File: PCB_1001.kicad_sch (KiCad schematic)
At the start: 3 parts

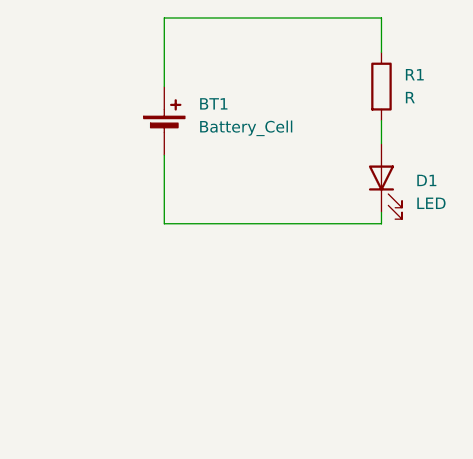
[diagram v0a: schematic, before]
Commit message: VTPN applied, incl footprints
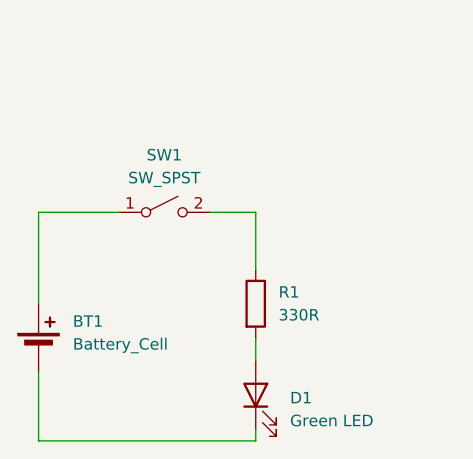
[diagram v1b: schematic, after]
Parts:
- added SW1: SW_SPST, symbol Switch:SW_SPST
- D1: value LED -> Green LED; footprint (none) -> LED_SMD:LED_0805_2012Metric; MFG (none) -> Dialight; MPN (none) -> 598-8181-102F; VTPN (none) -> 4752-01010-00
- R1: value R -> 330R; footprint (none) -> Resistor_SMD:R_0603_1608Metric; MFG (none) -> Yageo; MPN (none) -> RC0603FR-07330RL; VTPN (none) -> 4006-00040-00
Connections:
- net at R1.1: now also SW1.2 (B); no longer BT1.1 (+)
- new net: BT1.1 (+), SW1.1 (A)
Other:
- moved on the sheet: BT1, D1, R1
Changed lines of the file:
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@@
 	(wire
 		(pts
-			(xy 149.86 64.77) (xy 173.99 64.77)
-		)
-		(stroke
-			(width 0)
-			(type default)
-		)
-	)
-	(wire
-		(pts
-			(xy 173.99 64.77) (xy 173.99 68.58)
-		)
-		(stroke
-			(width 0)
-			(type default)
-		)
-	)
-	(wire
-		(pts
-			(xy 173.99 86.36) (xy 173.99 87.63)
-		)
-		(stroke
-			(width 0)
-			(type default)
-		)
-	)
-	(wire
-		(pts
-			(xy 149.86 87.63) (xy 149.86 80.01)
-		)
-		(stroke
-			(width 0)
-			(type default)
-		)
-	)
-	(wire
-		(pts
-			(xy 173.99 87.63) (xy 149.86 87.63)
-		)
-		(stroke
-			(width 0)
-			(type default)
-		)
-	)
-	(wire
-		(pts
-			(xy 149.86 72.39) (xy 149.86 64.77)
-		)
-		(stroke
-			(width 0)
-			(type default)
-		)
-	)
-	(wire
-		(pts
-			(xy 173.99 76.2) (xy 173.99 78.74)
+			(xy 160.02 110.49) (xy 160.02 111.76)
+		)
+		(stroke
+			(width 0)
+			(type default)
+		)
+	)
+	(wire
+		(pts
+			(xy 135.89 111.76) (xy 135.89 104.14)
+		)
+		(stroke
+			(width 0)
+			(type default)
+		)
+	)
+	(wire
+		(pts
+			(xy 160.02 111.76) (xy 135.89 111.76)
+		)
+		(stroke
+			(width 0)
+			(type default)
+		)
+	)
+	(wire
+		(pts
+			(xy 154.94 86.36) (xy 160.02 86.36)
+		)
+		(stroke
+			(width 0)
+			(type default)
+		)
+	)
+	(wire
+		(pts
+			(xy 135.89 86.36) (xy 135.89 96.52)
+		)
+		(stroke
+			(width 0)
+			(type default)
+		)
+	)
+	(wire
+		(pts
+			(xy 160.02 100.33) (xy 160.02 102.87)
+		)
+		(stroke
+			(width 0)
+			(type default)
+		)
+	)
+	(wire
+		(pts
+			(xy 144.78 86.36) (xy 135.89 86.36)
+		)
+		(stroke
+			(width 0)
+			(type default)
+		)
+	)
+	(wire
+		(pts
+			(xy 160.02 86.36) (xy 160.02 92.71)
 		)
 		(stroke
@@
 	(symbol
 		(lib_id "Device:R")
-		(at 173.99 72.39 0)
+		(at 160.02 96.52 0)
 		(unit 1)
 		(exclude_from_sim no)
@@
 		(fields_autoplaced yes)
 		(property "Reference" "R1"
-			(at 176.53 71.1199 0)
+			(at 162.56 95.2499 0)
 			(effects
 				(font
@@
 			)
 		)
-		(property "Value" "R"
-			(at 176.53 73.6599 0)
+		(property "Value" "330R"
+			(at 162.56 97.7899 0)
 			(effects
 				(font
@@
 			)
 		)
-		(property "Footprint" ""
-			(at 172.212 72.39 90)
-			(effects
-				(font
-					(size 1.27 1.27)
-				)
-				(hide yes)
-			)
-		)
-		(property "Datasheet" "~"
-			(at 173.99 72.39 0)
-			(effects
-				(font
-					(size 1.27 1.27)
-				)
-				(hide yes)
-			)
-		)
-		(property "Description" "Resistor"
-			(at 173.99 72.39 0)
+		(property "Footprint" "Resistor_SMD:R_0603_1608Metric"
+			(at 158.242 96.52 90)
+			(effects
+				(font
+					(size 1.27 1.27)
+				)
+				(hide yes)
+			)
+		)
+		(property "Datasheet" "https://www.yageo.com/upload/media/product/products/datasheet/rchip/PYu-RC_Group_51_RoHS_L_12.pdf"
+			(at 160.02 96.52 0)
+			(effects
+				(font
+					(size 1.27 1.27)
+				)
+				(hide yes)
+			)
+		)
+		(property "Description" "330 Ohms ±1% 0.1W, 1/10W Chip Resistor 0603 (1608 Metric) Moisture Resistant Thick Film"
+			(at 160.02 96.52 0)
+			(effects
+				(font
+					(size 1.27 1.27)
+				)
+				(hide yes)
+			)
+		)
+		(property "MFG" "Yageo"
+			(at 160.02 96.52 0)
+			(effects
+				(font
+					(size 1.27 1.27)
+				)
+				(hide yes)
+			)
+		)
+		(property "MPN" "RC0603FR-07330RL"
+			(at 160.02 96.52 0)
+			(effects
+				(font
+					(size 1.27 1.27)
+				)
+				(hide yes)
+			)
+		)
+		(property "VTPN" "4006-00040-00"
+			(at 160.02 96.52 0)
 			(effects
 				(font
@@
 	)
 	(symbol
+		(lib_id "Switch:SW_SPST")
+		(at 149.86 86.36 0)
+		(unit 1)
+		(exclude_from_sim no)
+		(in_bom yes)
+		(on_board yes)
+		(dnp no)
+		(fields_autoplaced yes)
+		(property "Reference" "SW1"
+			(at 149.86 80.01 0)
+			(effects
+				(font
+					(size 1.27 1.27)
+				)
+			)
+		)
+		(property "Value" "SW_SPST"
+			(at 149.86 82.55 0)
+			(effects
+				(font
+					(size 1.27 1.27)
+				)
+			)
+		)
+		(property "Footprint" ""
+			(at 149.86 86.36 0)
+			(effects
+				(font
+					(size 1.27 1.27)
+				)
+				(hide yes)
+			)
+		)
+		(property "Datasheet" "~"
+			(at 149.86 86.36 0)
+			(effects
+				(font
+					(size 1.27 1.27)
+				)
+				(hide yes)
+			)
+		)
+		(property "Description" "Single Pole Single Throw (SPST) switch"
+			(at 149.86 86.36 0)
+			(effects
+				(font
+					(size 1.27 1.27)
+				)
+				(hide yes)
+			)
+		)
+		(pin "1"
+		)
+		(pin "2"
+		)
+		(instances
+			(project ""
+				(path "/22a5288a-bb92-439e-beb9-11eba2442c24"
+					(reference "SW1")
+					(unit 1)
+				)
+			)
+		)
+	)
+	(symbol
 		(lib_id "Device:Battery_Cell")
-		(at 149.86 77.47 0)
+		(at 135.89 101.6 0)
 		(unit 1)
 		(exclude_from_sim no)
@@
 		(fields_autoplaced yes)
 		(property "Reference" "BT1"
-			(at 153.67 74.3584 0)
+			(at 139.7 98.4884 0)
 			(effects
 				(font
@@
 		)
 		(property "Value" "Battery_Cell"
-			(at 153.67 76.8984 0)
+			(at 139.7 101.0284 0)
 			(effects
 				(font
@@
 		)
 		(property "Footprint" ""
-			(at 149.86 75.946 90)
+			(at 135.89 100.076 90)
 			(effects
 				(font
@@
 		)
 		(property "Datasheet" "~"
-			(at 149.86 75.946 90)
+			(at 135.89 100.076 90)
 			(effects
 				(font
@@
 		)
 		(property "Description" "Single-cell battery"
-			(at 149.86 77.47 0)
+			(at 135.89 101.6 0)
 			(effects
 				(font
@@
 	(symbol
 		(lib_id "Device:LED")
-		(at 173.99 82.55 90)
+		(at 160.02 106.68 90)
 		(unit 1)
 		(exclude_from_sim no)
@@
 		(fields_autoplaced yes)
 		(property "Reference" "D1"
-			(at 177.8 82.8674 90)
+			(at 163.83 106.9974 90)
 			(effects
 				(font
@@
 			)
 		)
-		(property "Value" "LED"
-			(at 177.8 85.4074 90)
+		(property "Value" "Green LED"
+			(at 163.83 109.5374 90)
 			(effects
 				(font
@@
 			)
 		)
-		(property "Footprint" ""
-			(at 173.99 82.55 0)
-			(effects
-				(font
-					(size 1.27 1.27)
-				)
-				(hide yes)
-			)
-		)
-		(property "Datasheet" "~"
-			(at 173.99 82.55 0)
-			(effects
-				(font
-					(size 1.27 1.27)
-				)
-				(hide yes)
-			)
-		)
-		(property "Description" "Light emitting diode"
-			(at 173.99 82.55 0)
-			(effects
-				(font
+		(property "Footprint" "LED_SMD:LED_0805_2012Metric"
+			(at 160.02 106.68 0)
+			(effects
+				(font
+					(size 1.27 1.27)
+				)
+				(hide yes)
+			)
+		)
+		(property "Datasheet" "https://mm.digikey.com/Volume0/opasdata/d220001/medias/docus/511/598_Series_0805_Pkg.pdf"
+			(at 160.02 106.68 0)
+			(effects
+				(font
+					(size 1.27 1.27)
+				)
+				(hide yes)
+			)
+		)
+		(property "Description" "LED, Green 523nm, 3.2V, 0805 (2012 Metric)"
+			(at 160.02 106.68 0)
+			(effects
+				(font
+					(size 1.27 1.27)
+				)
+				(hide yes)
+			)
+		)
+		(property "MFG" "Dialight"
+			(at 160.02 106.68 90)
+			(effects
+				(font
+					(size 1.27 1.27)
+				)
+				(hide yes)
+			)
+		)
+		(property "MPN" "598-8181-102F"
+			(at 160.02 106.68 90)
+			(effects
+				(font
+					(size 1.27 1.27)
+				)
+				(hide yes)
+			)
+		)
+		(property "VTPN" "4752-01010-00"
+			(at 160.02 106.68 90)
+			(effects
+				(font

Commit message: Update Remote to match local
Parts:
- BT1: value Battery_Cell -> HPC 3v67; footprint (none) -> Battery:Battery_Panasonic_CR2032-HFN_Horizontal_CircularHoles; MFG (none) -> LongSing Technology; MPN (none) -> HPC-1520; VTPN (none) -> 4200-00020-00
- SW1: footprint (none) -> Button_Switch_SMD:SW_SPST_REED_CT10-XXXX-G1; MFG (none) -> Coto Technology; MPN (none) -> CT10-1030-G1; VTPN (none) -> 4751-00020-00
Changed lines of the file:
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@@
 			)
 		)
-		(property "Footprint" ""
+		(property "Footprint" "Button_Switch_SMD:SW_SPST_REED_CT10-XXXX-G1"
 			(at 149.86 86.36 0)
 			(effects
@@
 			)
 		)
-		(property "Datasheet" "~"
+		(property "Datasheet" "https://cototechnology.com/wp-content/uploads/2014/09/CotoClassic-CT10-Datasheet.pdf"
 			(at 149.86 86.36 0)
 			(effects
@@
 			)
 		)
-		(property "Description" "Single Pole Single Throw (SPST) switch"
+		(property "Description" "Reed Switch SPST-NO 10 ~ 30AT Operate Range 10W 500mA (AC/DC) 140 V SMD"
+			(at 149.86 86.36 0)
+			(effects
+				(font
+					(size 1.27 1.27)
+				)
+				(hide yes)
+			)
+		)
+		(property "MFG" "Coto Technology"
+			(at 149.86 86.36 0)
+			(effects
+				(font
+					(size 1.27 1.27)
+				)
+				(hide yes)
+			)
+		)
+		(property "MPN" "CT10-1030-G1"
+			(at 149.86 86.36 0)
+			(effects
+				(font
+					(size 1.27 1.27)
+				)
+				(hide yes)
+			)
+		)
+		(property "VTPN" "4751-00020-00"
 			(at 149.86 86.36 0)
 			(effects
@@
 			)
 		)
-		(property "Value" "Battery_Cell"
+		(property "Value" "HPC 3v67"
 			(at 139.7 101.0284 0)
 			(effects
@@
 			)
 		)
-		(property "Footprint" ""
+		(property "Footprint" "Battery:Battery_Panasonic_CR2032-HFN_Horizontal_CircularHoles"
 			(at 135.89 100.076 90)
 			(effects
@@
 			)
 		)
-		(property "Datasheet" "~"
+		(property "Datasheet" "https://www.longsingtechnology.com/product/hpc1520/"
 			(at 135.89 100.076 90)
 			(effects
@@
 			(at 135.89 101.6 0)
 			(effects
+				(font
+					(size 1.27 1.27)
+				)
+				(hide yes)
+			)
+		)
+		(property "MFG" "LongSing Technology"
+			(at 135.89 101.6 0)
+			(effects
+				(font
+					(size 1.27 1.27)
+				)
+				(hide yes)
+			)
+		)
+		(property "MPN" "HPC-1520"
+			(at 135.89 101.6 0)
+			(effects
+				(font
+					(size 1.27 1.27)
+				)
+				(hide yes)
+			)
+		)
+		(property "VTPN" "4200-00020-00"
+			(at 135.89 101.6 0)
+			(effects
